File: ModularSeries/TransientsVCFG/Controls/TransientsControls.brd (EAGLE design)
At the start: 99 x 100 mm, 25 parts, among them SW1 PVA1_DPST, SW2 PVA2_DPDT, SW3 PVA1_DPST, SW4 PVA2_DPDT

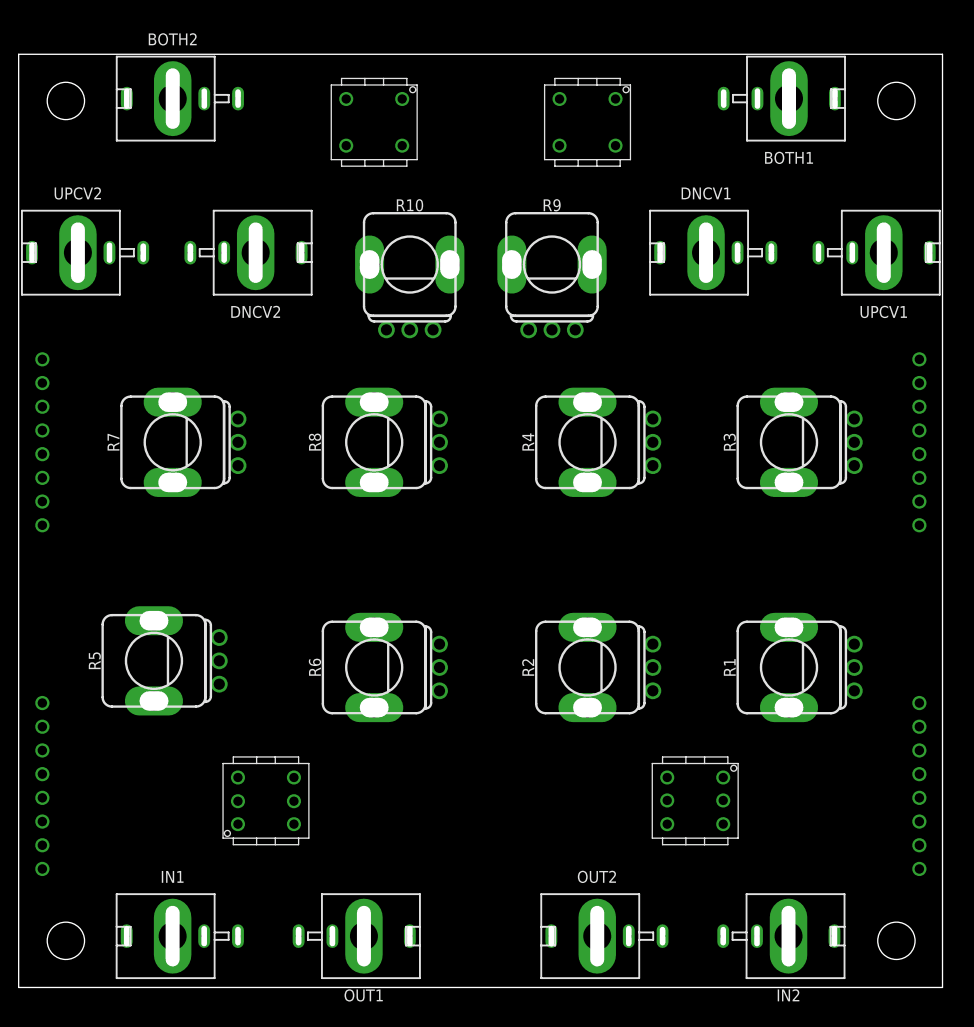
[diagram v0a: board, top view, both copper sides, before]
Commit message: Folder cleaned up, Transients added
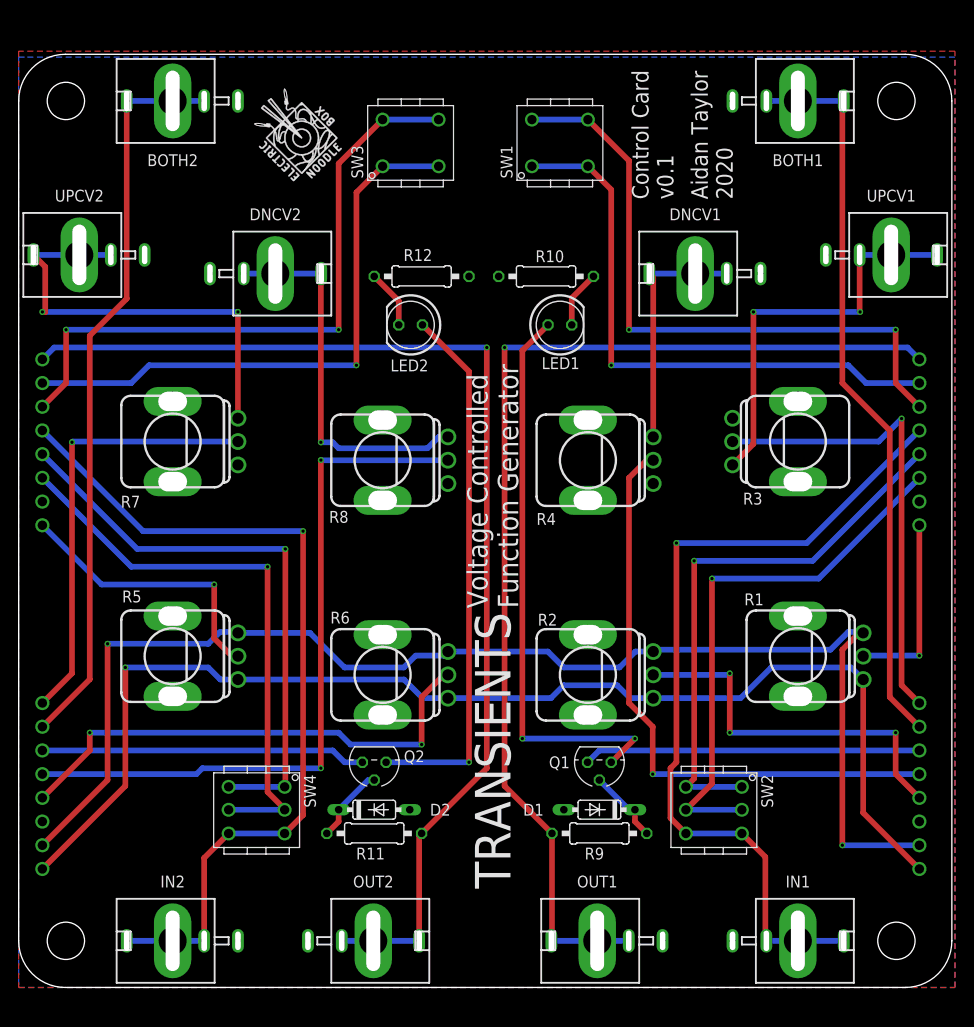
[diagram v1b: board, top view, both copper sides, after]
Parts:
- added D1, D2: (no value), ElectricNoodleBox:DO35-7
- added LED1, LED2: (no value), led:LED5MM
- added Q1, Q2: 2N3904, transistor-neu-to92:TO92
- added R11, R12: (no value), rcl:0207/10
- added U$1, U$2: (no value), ElectricNoodleBox:LOGO10X10
- R10, R9: device ElectricNoodleBox:ALPHA_RV09_9MMPOT -> rcl:0207/10
- moved IN1 67.0 mm to (83.5, 5.00), turned to 270 degrees
- moved IN2 66.0 mm to (16.5, 5.00), turned to 90 degrees
- moved R9 61.2 mm to (62.2, 16.5)
- moved OUT1 25.0 mm to (62.0, 5.00), turned to 90 degrees
- moved OUT2 24.0 mm to (38.0, 5.00), turned to 270 degrees
- moved R10 14.7 mm to (56.5, 76.2)
- moved SW3 4.48 mm to (42.0, 90.5), turned to 0 degrees
- moved SW1 3.69 mm to (58.0, 90.5), turned to 0 degrees
- moved DNCV2 3.07 mm to (27.5, 76.5)
- moved DNCV1 2.52 mm to (72.5, 76.5)
- moved SW2 2.24 mm to (74.5, 19.0)
- moved R8 2.12 mm to (39.0, 56.5)
- moved R5 2.06 mm to (16.5, 35.5)
- moved R4 1.92 mm to (61.0, 56.5)
- moved R1 1.54 mm to (83.5, 35.5)
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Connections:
- removed net N$9: B1.OUT2, OUT2.CONN, OUT2.T1, OUT2.T2
- new net N$27: LED1.K, R10.2
- new net N$28: D2.C, Q2.2, R11.2
- new net N$29: LED2.A, Q2.3
- new net N$30: LED2.K, R12.2
- new net N$31: B1.+12V2, Q2.1
- new net OUT2: B1.OUT2, OUT2.CONN, OUT2.T1, OUT2.T2, R11.1
- net GNDA: now also D1.A, D2.A, R1.LUGL, R1.LUGR, R10.1, R12.1, R2.LUGL, R2.LUGR, R3.LUGL, R3.LUGR, R4.LUGL, R4.LUGR, R5.LUGL, R5.LUGR, R6.LUGL, R6.LUGR, R7.LUGL, R7.LUGR, R8.LUGL, R8.LUGR; no longer R10.C1, R9.C1
- net N$1: now also B1.+12V1, Q1.1; no longer B1.OUT1, OUT1.CONN, OUT1.T1, OUT1.T2
- net N$25: now also D1.C, Q1.2, R9.2; no longer B1.DSHP1, B1.USHP1, R9.C2
- net N$26: now also LED1.A, Q1.3; no longer B1.DSHP2, B1.USHP2, R10.C2
- net OUT1: now also B1.OUT1, OUT1.CONN, OUT1.T1, OUT1.T2, R9.1; no longer R10.C3, R9.C3
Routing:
- net V+: track 0.00 -> 142.9 mm, vias 0 -> 2
- net V-: track 0.00 -> 131.5 mm, vias 0 -> 1
- net OUT2: track 0.00 -> 123.0 mm, vias 0 -> 1
- net OUT1: track 0.00 -> 119.0 mm, vias 0 -> 1
- net INPUT2: track 0.00 -> 92.5 mm, vias 0 -> 1
- net INPUT1: track 0.00 -> 90.0 mm, vias 0 -> 1
- net N$20: track 0.00 -> 79.1 mm
- net N$7: track 0.00 -> 78.8 mm
- net N$19: track 0.00 -> 76.7 mm, vias 0 -> 2
- net N$22: track 0.00 -> 69.0 mm, vias 0 -> 2
- net N$13: track 0.00 -> 68.2 mm, vias 0 -> 2
- net N$8: track 0.00 -> 64.8 mm, vias 0 -> 1
- net N$21: track 0.00 -> 62.9 mm, vias 0 -> 1
- net N$12: track 0.00 -> 62.2 mm, vias 0 -> 1
- net N$23: track 0.00 -> 61.8 mm, vias 0 -> 1
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- added copper zone on layer 1, net GNDA
- added copper zone on layer 16, net GNDA
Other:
- board size 99 x 100 mm -> 100 x 100 mm
- board text added: "Aidan Taylor 2020"
- board text added: "Control Card v0.1"
- board text added: "TRANSIENTS"
- board text added: "Voltage Controlled Function Generator"

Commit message: All active BOMs updated to new header standard
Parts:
- D1, D2: value (none) -> BAT85
- LED1, LED2: value (none) -> red_5MM
- R1, R2, R5, R6: value (none) -> B100K
- R10, R11, R12, R9: value (none) -> 1K
- R3, R4, R7, R8: value (none) -> B10K
